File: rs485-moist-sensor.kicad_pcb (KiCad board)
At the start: 2 copper layers, 18 x 149 mm, 31 parts, among them IC1 ATTINY441-SSU, P1 AVR ISP6, P2 CONN_01X04, Q1 Q_PMOS_GSD, U1 SN65HVD72, U2 MCP1702, X1 16MHz

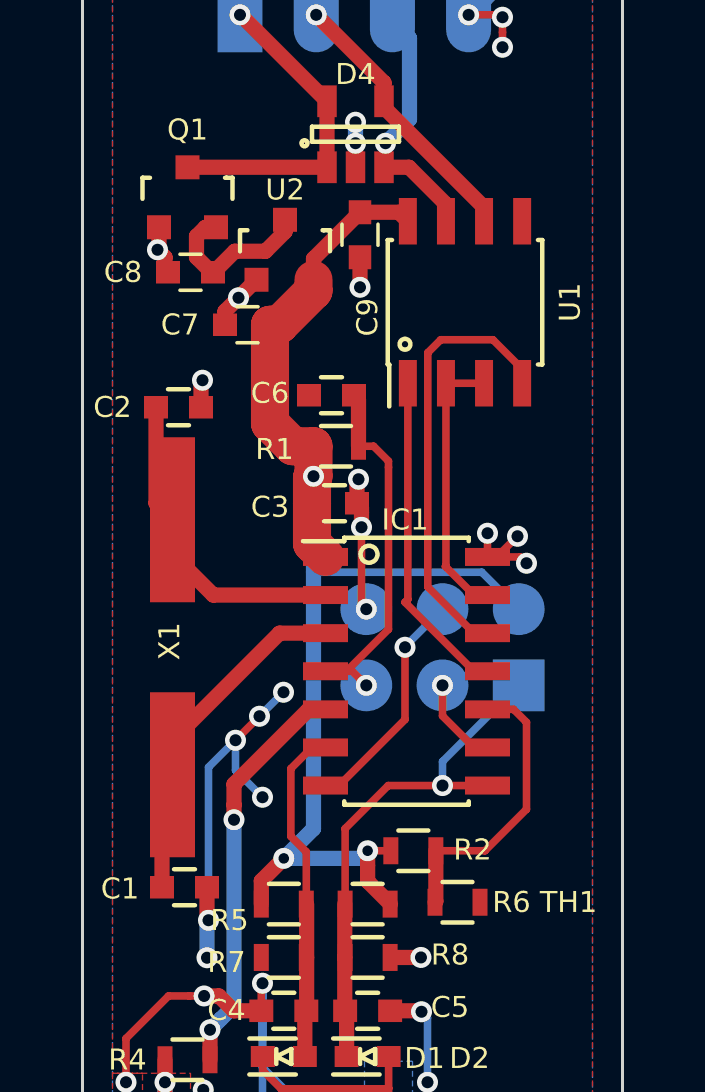
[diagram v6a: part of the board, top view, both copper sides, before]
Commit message: Pullup/pulldown resistors to put rs485 transceiver in off mode by default. Connect DE, ~RE lines to MCU separately. Provide power to resistive dividers from MCU, not from regulator to allow for lower power consumption
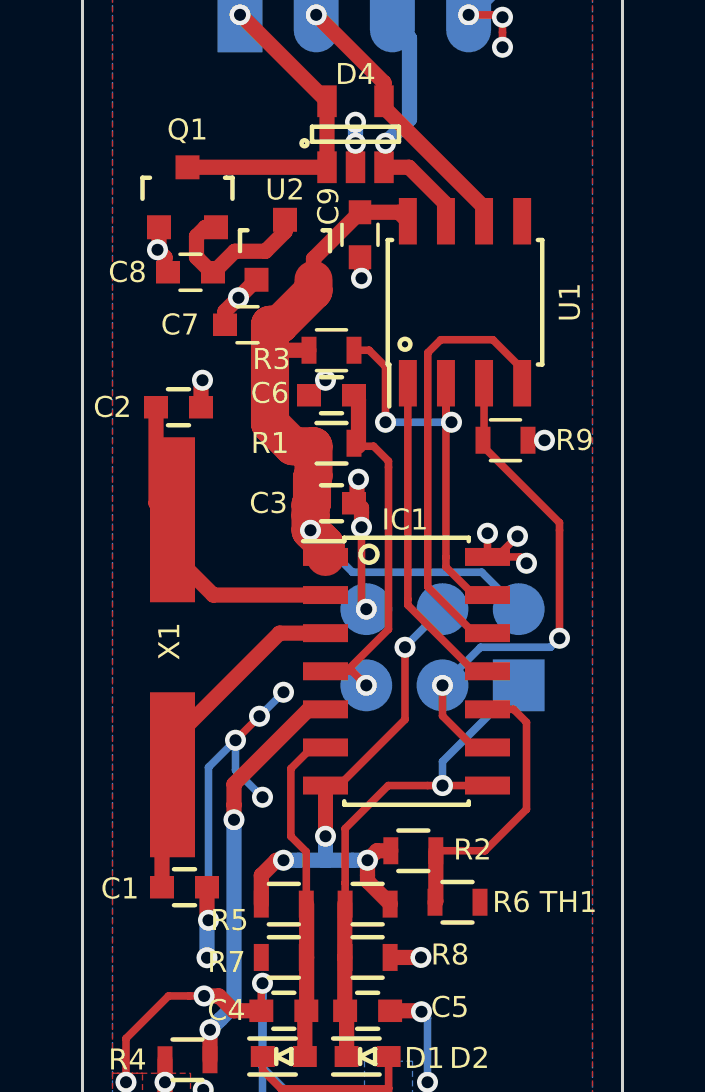
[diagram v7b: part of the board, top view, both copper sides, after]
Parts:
- added R3: 10k, Resistors_SMD:R_0603, F.Cu at (94.3, 33.1)
- added R9: 10k, Resistors_SMD:R_0603, F.Cu at (100.1, 36.1)
- C1, C2: value 18p -> 33p
- P1: value AVR ISP6 -> CONN_02X03
- moved R1 0.18 mm to (94.3, 36.2)
- moved C3 0.10 mm to (94.3, 38.2)
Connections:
- net Net-(IC1-Pad11) renamed /RX
- net Net-(IC1-Pad12) renamed /TX
- IC1 pad 13: Net-(IC1-Pad13) -> /RS485_READER_ENABLE
- R2 pad 1: +3V3 -> /MOSI
- R5 pad 2: +3V3 -> /MOSI
- R6 pad 2: +3V3 -> /MOSI
- U1 pad 2: Net-(IC1-Pad13) -> /RS485_READER_ENABLE
- U1 pad 3: Net-(IC1-Pad13) -> /SCK
- U1 pad 5: GND -> Net-(U1-Pad5)
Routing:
- net +3V3: track 44.2 -> 25.2 mm, vias 3 -> 1
- net /RS485_READER_ENABLE: track 0.00 -> 14.6 mm, vias 0 -> 2
- net /SCK: track 2.95 -> 17.1 mm, vias 1 -> 2
- net /MOSI: track 7.76 -> 17.6 mm, vias 1 -> 4
- net Net-(IC1-Pad13): track 9.18 -> 0.00 mm
- net GND: track 222.1 -> 222.7 mm, vias 150 -> 152

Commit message: Fix a missing ground connection. Make PCB updatable from schematics directly
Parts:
- MK1, MK2: renamed from REF**; value MountingHole_3mm -> Mounting_Hole
- renumbered G*** to #G***, G*** to #LOGO1
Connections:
- U1 pad 5: Net-(U1-Pad5) -> GND
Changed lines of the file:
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@@
-(kicad_pcb (version 20170123) (host pcbnew no-vcs-found-4b5482e~58~ubuntu16.04.1)
+(kicad_pcb (version 20170123) (host pcbnew no-vcs-found-1466d0c~58~ubuntu16.04.1)
   (general
-    (links 67)
+    (links 68)
     (no_connects 0)
     (area 83.111667 11.868 114.755 163.400001)
@@
     (zones 0)
     (modules 33)
-    (nets 21)
+    (nets 20)
   )
   (page A4)
@@
   (net 18 /TX)
   (net 19 /RS485_READER_ENABLE)
-  (net 20 "Net-(U1-Pad5)")
   (net_class Default "This is the default net class."
     (clearance 0.1778)
@@
     (add_net "Net-(C2-Pad1)")
     (add_net "Net-(C8-Pad1)")
-    (add_net "Net-(U1-Pad5)")
     (add_net VCC)
   )
@@
       (net 15 /RS485A))
     (pad 5 smd rect (at 2.7 1.905 90) (size 1.55 0.6) (layers F.Cu F.Paste F.Mask)
-      (net 20 "Net-(U1-Pad5)"))
+      (net 2 GND))
     (pad 4 smd rect (at -2.7 1.905 90) (size 1.55 0.6) (layers F.Cu F.Paste F.Mask)
       (net 18 /TX))
@@
     (descr "Mounting hole, Befestigungsbohrung, 3mm, No Annular, Kein Restring,")
     (tags "Mounting hole, Befestigungsbohrung, 3mm, No Annular, Kein Restring,")
-    (fp_text reference REF** (at 0 -4.0005) (layer F.SilkS) hide
-      (effects (font (size 0.7 0.7) (thickness 0.11)))
-    )
-    (fp_text value MountingHole_3mm (at 1.00076 5.00126) (layer F.Fab)
+    (fp_text reference MK1 (at 0 -4.0005) (layer F.SilkS) hide
+      (effects (font (size 0.7 0.7) (thickness 0.11)))
+    )
+    (fp_text value Mounting_Hole (at 1.00076 5.00126) (layer F.Fab)
       (effects (font (size 0.7 0.7) (thickness 0.11)))
     )
@@
     (descr "Mounting hole, Befestigungsbohrung, 3mm, No Annular, Kein Restring,")
     (tags "Mounting hole, Befestigungsbohrung, 3mm, No Annular, Kein Restring,")
-    (fp_text reference REF** (at 0 -4.0005) (layer F.SilkS) hide
-      (effects (font (size 0.7 0.7) (thickness 0.11)))
-    )
-    (fp_text value MountingHole_3mm (at 1.00076 5.00126) (layer F.Fab)
+    (fp_text reference MK2 (at 0 -4.0005) (layer F.SilkS) hide
+      (effects (font (size 0.7 0.7) (thickness 0.11)))
+    )
+    (fp_text value Mounting_Hole (at 1.00076 5.00126) (layer F.Fab)
       (effects (font (size 0.7 0.7) (thickness 0.11)))
     )
@@
     (pad 1 thru_hole circle (at 0 0) (size 2.99974 2.99974) (drill 2.99974) (layers))
   )
-  (module w_logo:Logo_silk_OSHW_6x6mm (layer F.Cu)
+  (module w_logo:Logo_silk_OSHW_6x6mm locked (layer F.Cu)
     (at 95 103)
     (descr "Open Hardware Logo, 6x6mm")
-    (fp_text reference G*** (at 0 0) (layer F.SilkS) hide
+    (zone_connect 0)
+    (attr virtual)
+    (fp_text reference "#LOGO1" (at 0 0) (layer F.SilkS) hide
       (effects (font (size 0.7 0.7) (thickness 0.11)))
     )
@@
       (xy -1.51384 2.24536)) (layer F.SilkS) (width 0.00254))
   )
-  (module chirp_logo:ziogas (layer B.Cu)
+  (module chirp_logo:ziogas locked (layer B.Cu)
     (at 96.25 130 270)
-    (fp_text reference G*** (at 0 0 270) (layer B.SilkS) hide
+    (attr virtual)
+    (fp_text reference "#G***" (at 0 0 270) (layer B.SilkS) hide
       (effects (font (size 0.7 0.7) (thickness 0.11)) (justify mirror))
     )
@@
   (via (at 97.282 53.34) (size 0.7) (drill 0.4) (layers F.Cu B.Cu) (net 2))
   (segment (start 96.266 53.34) (end 97.282 53.34) (width 0.508) (layer F.Cu) (net 2))
+  (segment (start 100.655 28.8) (end 100.655 28.325) (width 0.254) (layer F.Cu) (net 2))
   (segment (start 88.45 35) (end 88.45 38.2) (width 0.508) (layer F.Cu) (net 3))
   (segment (start 88.45 38.2) (end 89 38.75) (width 0.508) (layer F.Cu) (net 3))
@@
   (segment (start 99.05 41.26) (end 98.115 40.325) (width 0.254) (layer F.Cu) (net 19))
   (segment (start 98.115 40.325) (end 98.115 40) (width 0.254) (layer F.Cu) (net 19))
-  (segment (start 100.655 28.8) (end 100.655 28.325) (width 0.254) (layer F.Cu) (net 20))
   (zone (net 2) (net_name GND) (layer B.Cu) (hatch edge 0.508)
     (connect_pads (clearance 0.254))
